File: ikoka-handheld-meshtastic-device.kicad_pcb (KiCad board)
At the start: 2 copper layers, 40 x 55 mm, 42 parts, among them J1 Conn_Coaxial, J4 1.25-2PWB, Q1 AO3401A, SW1 SW_Push, SW2 SW_Push, U1 MT3608B, U2 E22-900M30S, U3 XIAO-nRF52840-SMD, U4 TP4056-42-ESOP8

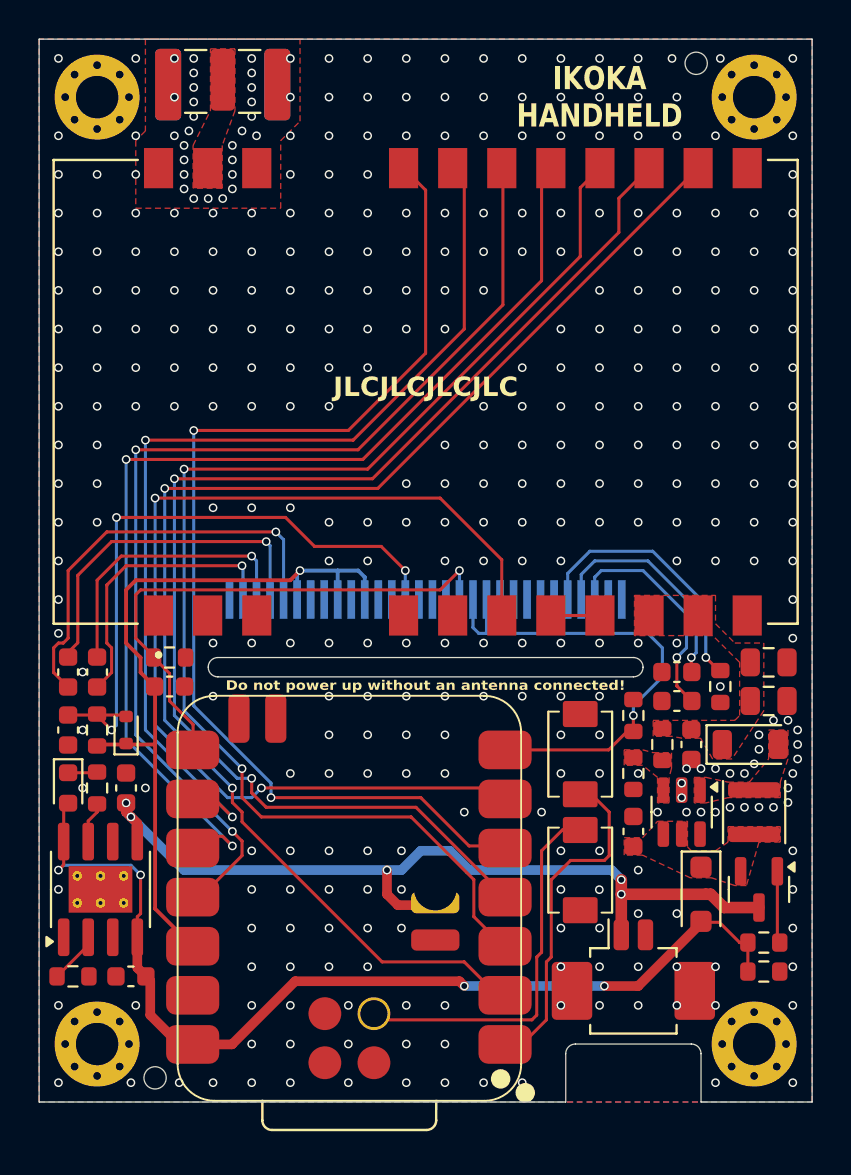
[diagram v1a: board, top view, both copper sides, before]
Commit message: feat: Boost converter improvements
- Change Schottky diode from DSK26 (Vf 0.7V, Iav 2A) to DSK34 (Vf 0.55V, Iav 3A)
- Change inductor from FNR3015S2R2MT (2.2µH, 2A/2A, DCR 0.06Ω) to FTC303018D4R7MBCA (4.7µH, 4.2A/3A, DCR 0.087Ω)

Signed-off-by: Andrew Yong <me@ndoo.sg>
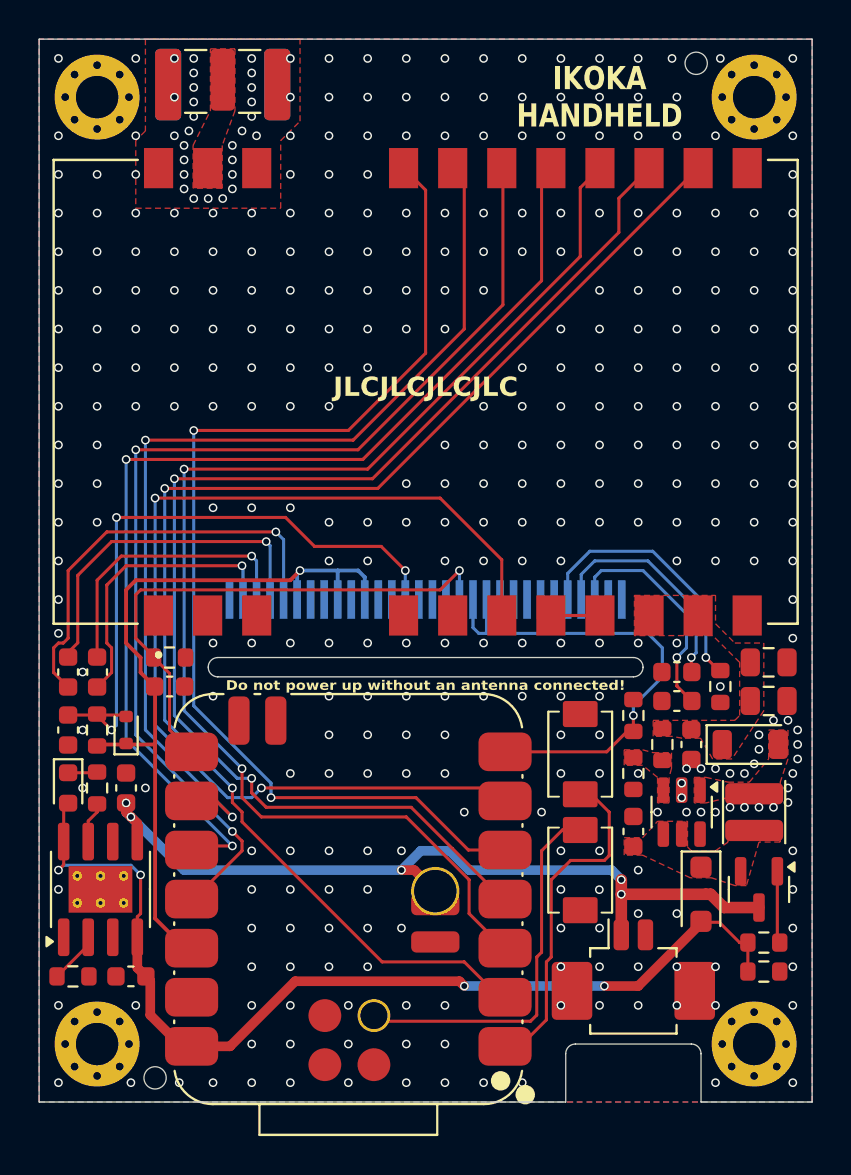
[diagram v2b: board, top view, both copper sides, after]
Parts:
- D1, D3: value DSK26 -> DSK34
- L1: value FNR3015S2R2MT -> FTC303018D4R7MBCA; footprint Inductor_SMD:L_Changjiang_FNR3015S -> Inductor_SMD:L_Changjiang_FTC303018D
- moved U3 0.10 mm to (146.0, 89.5)
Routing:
- net +BATT: track 45.6 -> 44.6 mm
- net GND: vias 380 -> 379

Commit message: fix: Remove I2C 4.7kΩ pull-down resistors - The resistors are wrongly wired as pull-down to GND instead of pull-up to 3V3, I2C is open drain and requires pull-up - Remove them entirely and rely on nrf52840 internal 13kΩ pull-up for I2C, this is sufficient for SSD1306 I2C speeds - Future addition of I2C external connector should provision pull-ups for stability
Fixes #3.

Signed-off-by: Andrew Yong <me@ndoo.sg>
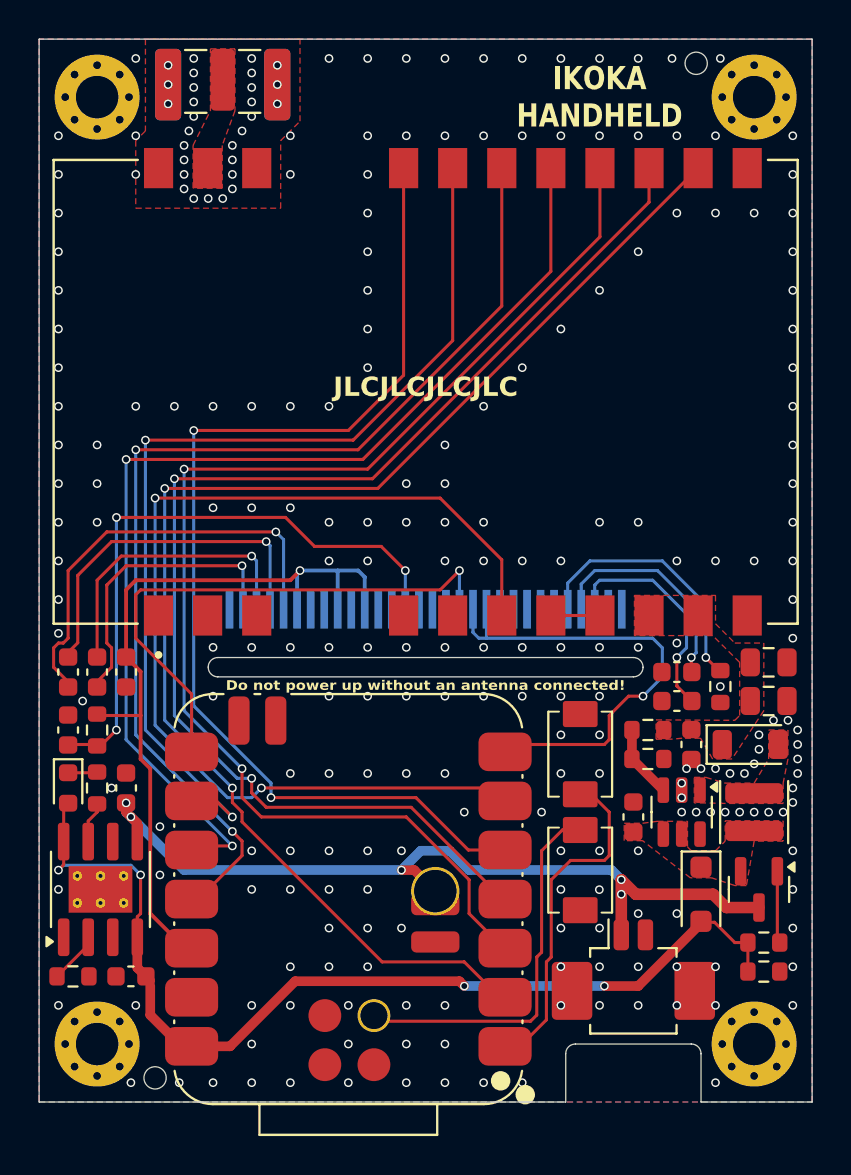
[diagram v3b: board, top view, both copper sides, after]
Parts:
- removed D2: 1N4148WT, Diode_SMD:D_SOD-523
- removed R6, R7: 4.7k, Resistor_SMD:R_0603_1608Metric
- C6: value 2.2uF -> 2.2uF 16V
- C8, C9: value 1uF -> 1uF 16V
- L1: value FTC303018D4R7MBCA -> FTC303020D4R7MBCA; footprint Inductor_SMD:L_Changjiang_FTC303018D -> Inductor_SMD:L_Changjiang_FTC303020D
- SYM1: footprint Symbol:OSHW-Logo_19x20mm_SilkScreen -> Symbol:OSHW-Logo_7.5x8mm_SilkScreen
- moved SYM1 11.3 mm to (139.0, 59.0)
- moved C5 2.37 mm to (134.5, 77.8), turned to -90 degrees
- moved R1 1.06 mm to (161.5, 80.8), turned to 180 degrees
- moved R2 1.06 mm to (161.5, 82.2), turned to 0 degrees
- moved C1 0.75 mm to (160.8, 85.2)
- moved DS1 0.50 mm to (150.0, 74.5)
- turned C10 to 90 degrees
- turned R8 to -90 degrees
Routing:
- net Net-(U1-FB): track 0.00 -> 3.79 mm
- net +3V3: track 40.3 -> 41.4 mm
- net Net-(DS1-~{RES}): track 32.9 -> 31.9 mm
- net /LORA_SPI_NSS: track 57.6 -> 56.6 mm
- net /I2C_SDA: track 25.5 -> 24.8 mm
- net Net-(DS1-C2P): track 14.8 -> 15.3 mm
- net Net-(DS1-C2N): track 14.9 -> 15.4 mm
- net Net-(DS1-C1P): track 18.0 -> 18.5 mm
- net /I2C_SCL: track 28.1 -> 28.6 mm
- net GND: track 0.21 -> 0.25 mm, vias 379 -> 254
- removed copper zone on F.Cu, net Net-(U1-FB)

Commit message: fix: Add 4.7kΩ pull-up resistors on I2C bus (fixes #5)
Signed-off-by: Andrew Yong <me@ndoo.sg>
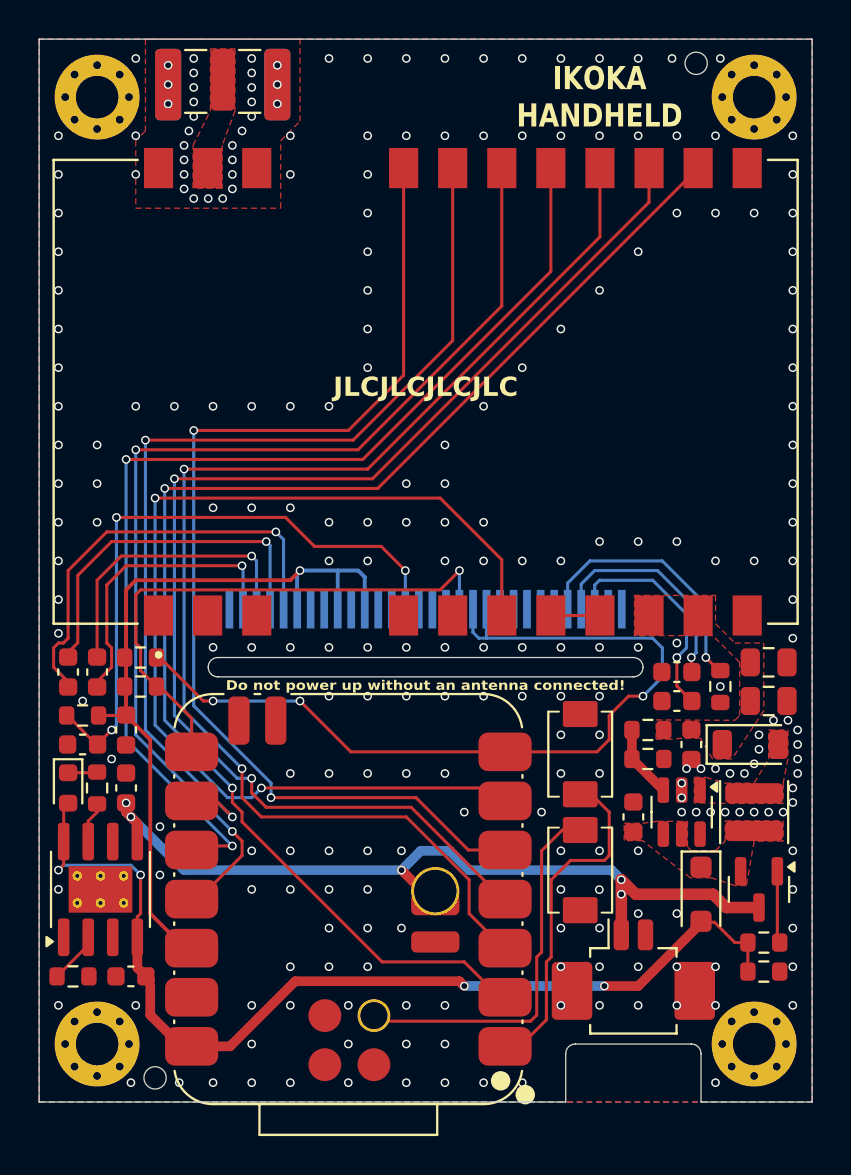
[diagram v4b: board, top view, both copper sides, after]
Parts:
- added R6: 4.7k, Resistor_SMD:R_0603_1608Metric, F.Cu at (135.2, 78.5)
- added R7: 4.7k, Resistor_SMD:R_0603_1608Metric, F.Cu at (135.2, 77.0)
- moved C5 3.00 mm to (134.5, 80.8)
- moved C10 1.06 mm to (132.2, 81.5), turned to 180 degrees
- moved R8 1.06 mm to (132.2, 80.0), turned to 180 degrees
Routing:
- net /I2C_SDA: track 24.8 -> 44.9 mm, vias 1 -> 3
- net +3V3: track 41.4 -> 40.2 mm
- net Net-(DS1-~{RES}): track 31.9 -> 32.4 mm
- net GND: track 0.25 -> 0.21 mm, vias 254 -> 253
